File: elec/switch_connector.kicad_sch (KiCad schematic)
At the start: 4 parts, among them J13 BM04B-SRSS-TB, Q2 AO3400A

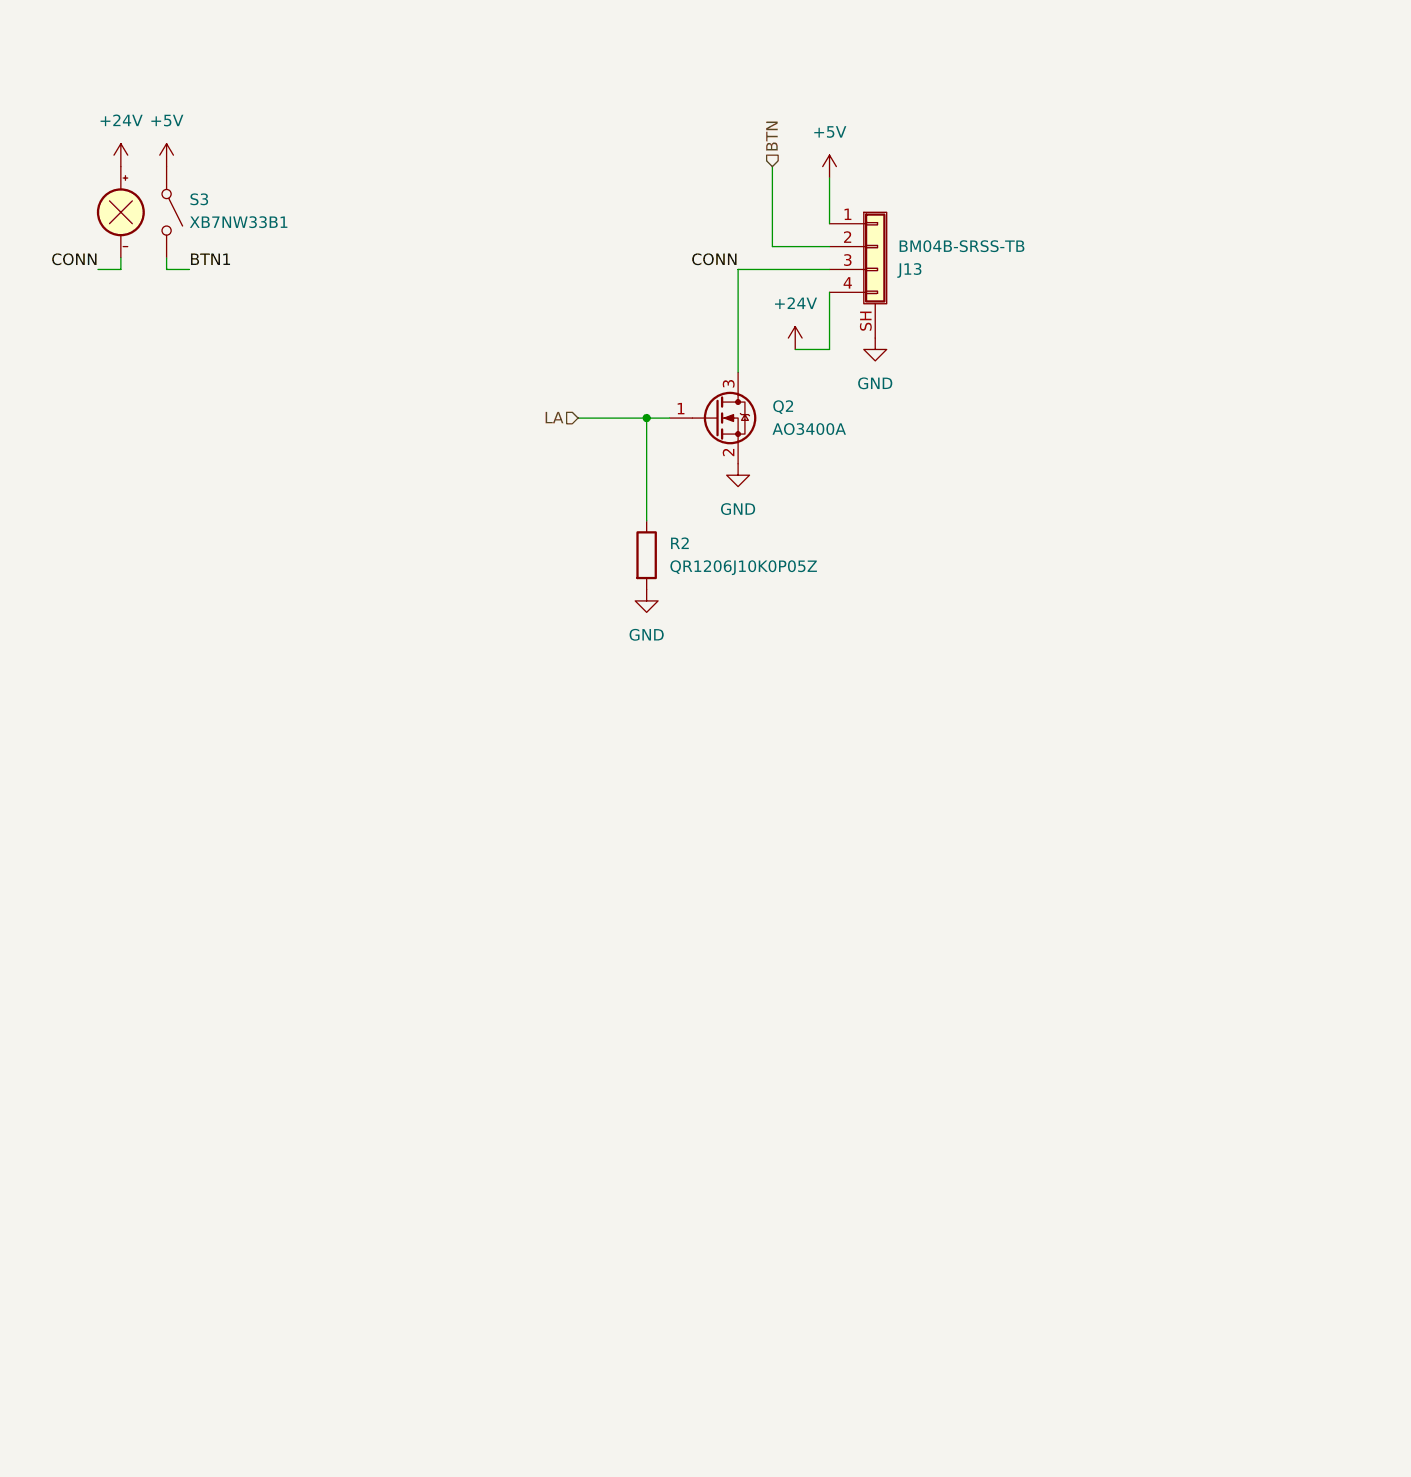
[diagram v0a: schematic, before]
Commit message: feat: adding modularity to PCB
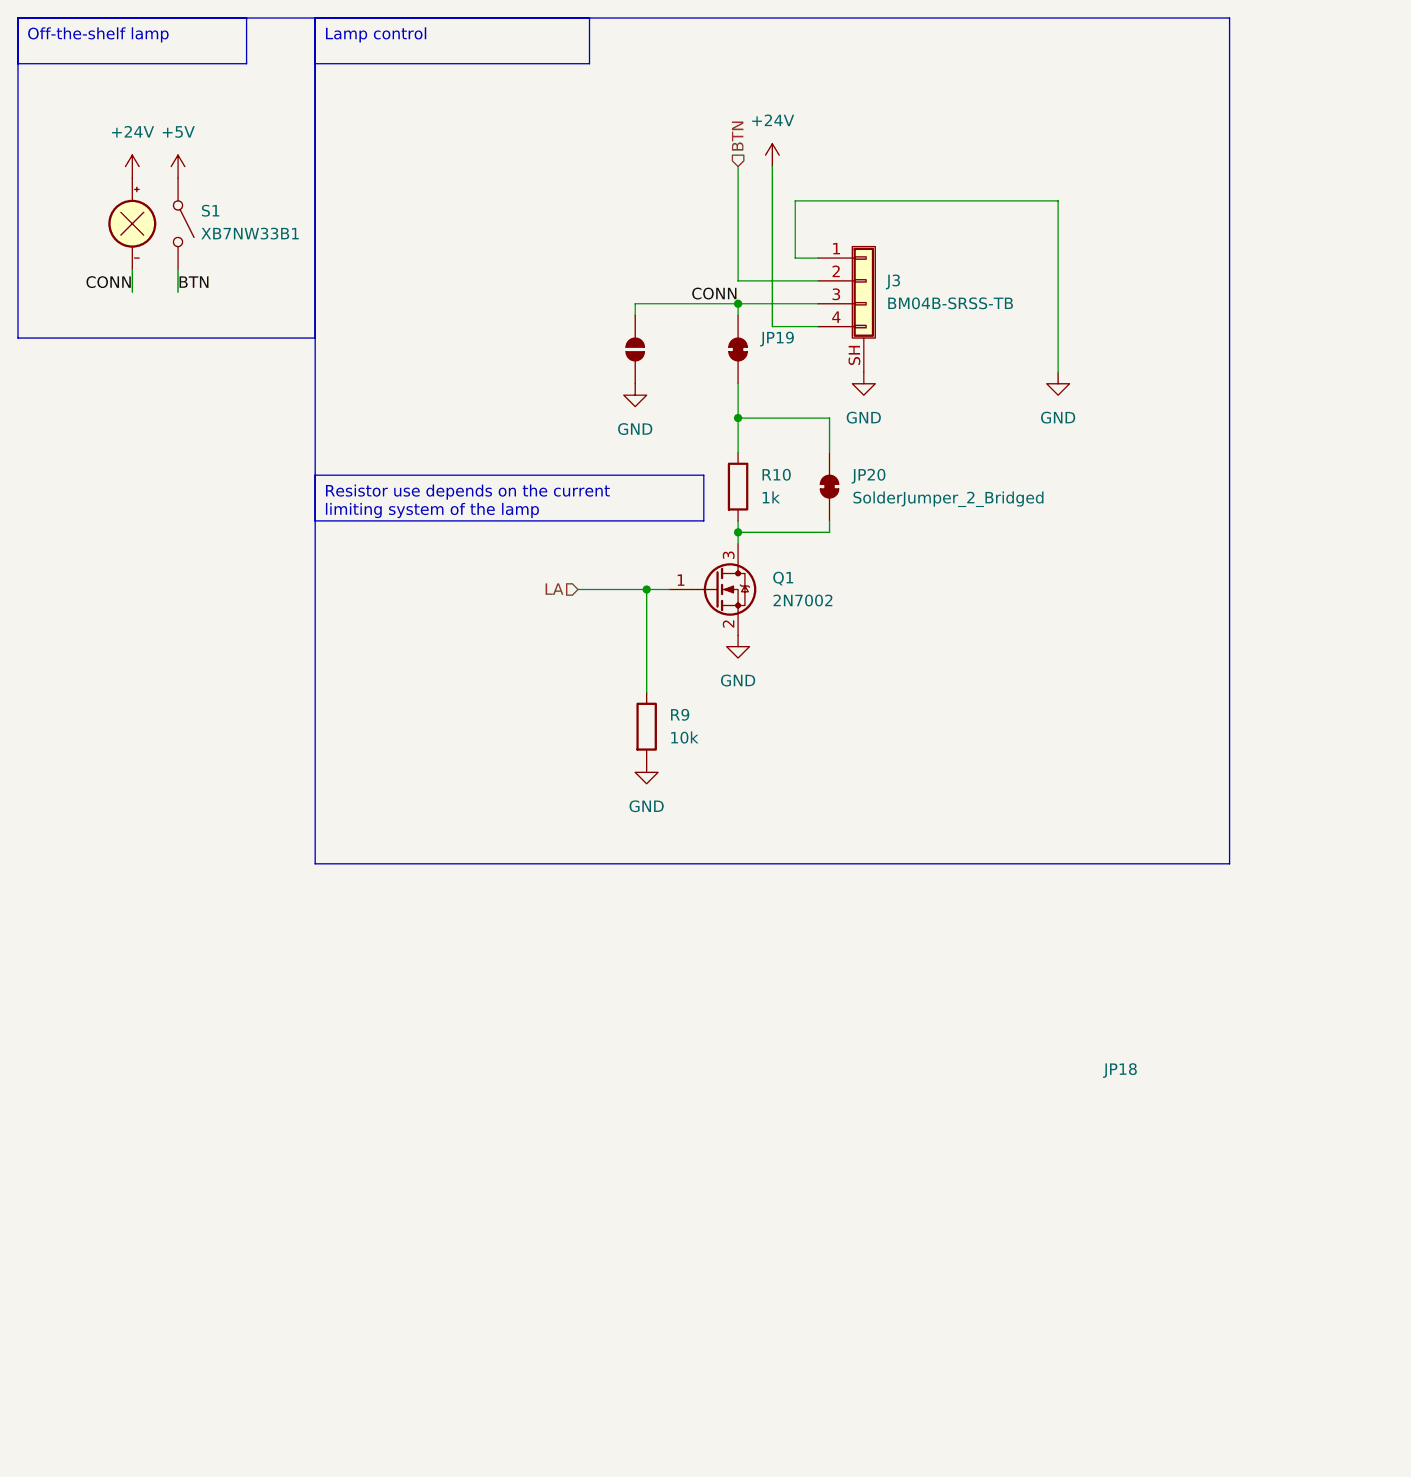
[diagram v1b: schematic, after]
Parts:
- removed Q2: AO3400A, Package_TO_SOT_SMD:SOT-23, symbol Transistor_FET:AO3400A
- added JP18: SolderJumper_2_Open, Jumper:SolderJumper-2_P1.3mm_Open_Pad1.0x1.5mm, symbol Jumper:SolderJumper_2_Open
- added JP19, JP20: SolderJumper_2_Bridged, Jumper:SolderJumper-2_P1.3mm_Bridged_Pad1.0x1.5mm, symbol Jumper:SolderJumper_2_Bridged
- added Q1: 2N7002, Package_TO_SOT_SMD:SOT-23, symbol Transistor_FET:2N7002
- added R10: 1k, Resistor_SMD:R_0805_2012Metric, symbol Device:R
- R9: renamed from R2; value QR1206J10K0P05Z -> 10k; footprint (none) -> Resistor_SMD:R_0805_2012Metric
- renumbered J13 to J3, S3 to S1
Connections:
- net BTN1 is gone; now on net BTN: S1.2 (14)
- net +5V: no longer J3.1 (Pin_1)
- net CONN: now also JP18.1 (A), JP19.2 (B)
- net GND: now also J3.1 (Pin_1), JP18.2 (B), Q1.2 (S)
- net LA: now also Q1.1 (G)
- new net: JP19.1 (A), JP20.2 (B), R10.1
- new net: JP20.1 (A), Q1.3 (D), R10.2
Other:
- moved on the sheet: J3, R9, S1

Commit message: v1 3D print PCB
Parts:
- removed JP19: SolderJumper_2_Bridged, Jumper:SolderJumper-2_P1.3mm_Bridged_Pad1.0x1.5mm, symbol Jumper:SolderJumper_2_Bridged
- renumbered JP20 to JP17
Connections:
- net CONN: now also JP17.2 (B), R10.1; no longer JP18.1 (A)
- net at JP17.1 (A), Q1.3 (D), R10.2: now also JP18.1 (A)
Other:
- moved on the sheet: JP17, JP18, R10

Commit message: doc: outline for fabrication guide
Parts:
- J3: MPN (none) -> C160390
- Q1: MPN (none) -> C8545
- R10: MPN (none) -> C17513
- R9: MPN (none) -> C17414
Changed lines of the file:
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@@
+			)
+		)
+		(property "MPN" "C17414"
+			(at 82.55 91.44 0)
+			(effects
+				(font
+					(size 1.27 1.27)
+				)
+				(hide yes)
 			)
 		)
@@
 			)
 		)
+		(property "MPN" "C8545"
+			(at 90.17 76.2 0)
+			(effects
+				(font
+					(size 1.27 1.27)
+				)
+				(hide yes)
+			)
+		)
 		(pin "1"
 		)
@@
 			)
 		)
+		(property "MPN" "C17513"
+			(at 92.71 63.5 0)
+			(effects
+				(font
+					(size 1.27 1.27)
+				)
+				(hide yes)
+			)
+		)
 		(pin "2"
 		)
@@
 			(at 106.68 41.91 0)
 			(effects
+				(font
+					(size 1.27 1.27)
+				)
+				(hide yes)
+			)
+		)
+		(property "MPN" "C160390"
+			(at 106.68 41.91 0)
+			(effects

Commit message: dev: updating pcb
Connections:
- net +5V is gone; now on net BTN: S1.1 (13)
- net BTN: no longer S1.2 (14)
- net GND: now also S1.2 (14)
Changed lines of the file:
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@@
 	(wire
 		(pts
-			(xy 25.4 43.18) (xy 25.4 40.64)
+			(xy 25.4 45.72) (xy 25.4 40.64)
 		)
 		(stroke
@@
 	(wire
 		(pts
-			(xy 30.48 43.18) (xy 30.48 40.64)
+			(xy 30.48 27.94) (xy 30.48 30.48)
 		)
 		(stroke
@@
 	)
 	(label "BTN"
-		(at 30.48 43.18 0)
+		(at 30.48 27.94 0)
 		(fields_autoplaced yes)
 		(effects
@@
 	)
 	(label "CONN"
-		(at 25.4 43.18 180)
+		(at 25.4 45.72 180)
 		(fields_autoplaced yes)
 		(effects
@@
 	)
 	(symbol
+		(lib_id "power:GND")
+		(at 30.48 40.64 0)
+		(unit 1)
+		(exclude_from_sim no)
+		(in_bom yes)
+		(on_board yes)
+		(dnp no)
+		(fields_autoplaced yes)
+		(property "Reference" "#PWR028"
+			(at 30.48 46.99 0)
+			(effects
+				(font
+					(size 1.27 1.27)
+				)
+				(hide yes)
+			)
+		)
+		(property "Value" "GND"
+			(at 30.48 45.72 0)
+			(effects
+				(font
+					(size 1.27 1.27)
+				)
+			)
+		)
+		(property "Footprint" ""
+			(at 30.48 40.64 0)
+			(effects
+				(font
+					(size 1.27 1.27)
+				)
+				(hide yes)
+			)
+		)
+		(property "Datasheet" ""
+			(at 30.48 40.64 0)
+			(effects
+				(font
+					(size 1.27 1.27)
+				)
+				(hide yes)
+			)
+		)
+		(property "Description" "Power symbol creates a global label with name \"GND\" , ground"
+			(at 30.48 40.64 0)
+			(effects
+				(font
+					(size 1.27 1.27)
+				)
+				(hide yes)
+			)
+		)
+		(pin "1"
+		)
+		(instances
+			(project "elec"
+				(path "/9721bce9-01f4-4230-bc1e-748d0303b61d/d1c63f12-a9c6-44fc-aada-0b6e04e33293"
+					(reference "#PWR028")
+					(unit 1)
+				)
+				(path "/9721bce9-01f4-4230-bc1e-748d0303b61d/5ed1a42c-1f8a-456f-aca4-b0ec53e5043f"
+					(reference "#PWR036")
+					(unit 1)
+				)
+				(path "/9721bce9-01f4-4230-bc1e-748d0303b61d/fdf19939-3d9b-4110-9022-c37157a29402"
+					(reference "#PWR044")
+					(unit 1)
+				)
+				(path "/9721bce9-01f4-4230-bc1e-748d0303b61d/37f927af-89ef-4fdd-8956-bca34548d96f"
+					(reference "#PWR052")
+					(unit 1)
+				)
+				(path "/9721bce9-01f4-4230-bc1e-748d0303b61d/986b1860-5bd6-47a5-b66e-b737b7bd0f11"
+					(reference "#PWR060")
+					(unit 1)
+				)
+				(path "/9721bce9-01f4-4230-bc1e-748d0303b61d/eebd9391-916f-49b6-bec7-88d6969a1573"
+					(reference "#PWR068")
+					(unit 1)
+				)
+				(path "/9721bce9-01f4-4230-bc1e-748d0303b61d/d67cbc77-a7b3-4445-bb70-2db77a7feb74"
+					(reference "#PWR076")
+					(unit 1)
+				)
+				(path "/9721bce9-01f4-4230-bc1e-748d0303b61d/3bc99195-9e3c-4290-911f-d629015a354c"
+					(reference "#PWR084")
+					(unit 1)
+				)
+				(path "/9721bce9-01f4-4230-bc1e-748d0303b61d/e3e2ca04-3651-46d9-8ec0-5b3aca5c73d2"
+					(reference "#PWR092")
+					(unit 1)
+				)
+				(path "/9721bce9-01f4-4230-bc1e-748d0303b61d/333f48b8-09d6-4cfc-b48e-393e968338e9"
+					(reference "#PWR0100")
+					(unit 1)
+				)
+			)
+		)
+	)
+	(symbol
 		(lib_id "breakout:XB7NW33B1")
 		(at 30.48 35.56 0)
@@
 					(unit 1)
 				)
-			)
-		)
-	)
-	(symbol
-		(lib_id "power:+5V")
-		(at 30.48 30.48 0)
-		(unit 1)
-		(exclude_from_sim no)
-		(in_bom yes)
-		(on_board yes)
-		(dnp no)
-		(fields_autoplaced yes)
-		(property "Reference" "#PWR028"
-			(at 30.48 34.29 0)
-			(effects
-				(font
-					(size 1.27 1.27)
-				)
-				(hide yes)
-			)
-		)
-		(property "Value" "+5V"
-			(at 30.48 25.4 0)
-			(effects
-				(font
-					(size 1.27 1.27)
-				)
-			)
-		)
-		(property "Footprint" ""
-			(at 30.48 30.48 0)
-			(effects
-				(font
-					(size 1.27 1.27)
-				)
-				(hide yes)
-			)
-		)
-		(property "Datasheet" ""
-			(at 30.48 30.48 0)
-			(effects
-				(font
-					(size 1.27 1.27)
-				)
-				(hide yes)
-			)
-		)
-		(property "Description" "Power symbol creates a global label with name \"+5V\""
-			(at 30.48 30.48 0)
-			(effects
-				(font
-					(size 1.27 1.27)
-				)
-				(hide yes)
-			)
-		)
-		(pin "1"
-		)
-		(instances
-			(project "elec"
-				(path "/9721bce9-01f4-4230-bc1e-748d0303b61d/d1c63f12-a9c6-44fc-aada-0b6e04e33293"
-					(reference "#PWR028")
-					(unit 1)
-				)
-				(path "/9721bce9-01f4-4230-bc1e-748d0303b61d/5ed1a42c-1f8a-456f-aca4-b0ec53e5043f"
-					(reference "#PWR036")
-					(unit 1)
-				)
-				(path "/9721bce9-01f4-4230-bc1e-748d0303b61d/fdf19939-3d9b-4110-9022-c37157a29402"
-					(reference "#PWR044")
-					(unit 1)
-				)
-				(path "/9721bce9-01f4-4230-bc1e-748d0303b61d/37f927af-89ef-4fdd-8956-bca34548d96f"
-					(reference "#PWR052")
-					(unit 1)
-				)
-				(path "/9721bce9-01f4-4230-bc1e-748d0303b61d/986b1860-5bd6-47a5-b66e-b737b7bd0f11"
-					(reference "#PWR060")
-					(unit 1)
-				)
-				(path "/9721bce9-01f4-4230-bc1e-748d0303b61d/eebd9391-916f-49b6-bec7-88d6969a1573"
-					(reference "#PWR068")
-					(unit 1)
-				)
-				(path "/9721bce9-01f4-4230-bc1e-748d0303b61d/d67cbc77-a7b3-4445-bb70-2db77a7feb74"
-					(reference "#PWR076")
-					(unit 1)
-				)
-				(path "/9721bce9-01f4-4230-bc1e-748d0303b61d/3bc99195-9e3c-4290-911f-d629015a354c"
-					(reference "#PWR084")
-					(unit 1)
-				)
-				(path "/9721bce9-01f4-4230-bc1e-748d0303b61d/e3e2ca04-3651-46d9-8ec0-5b3aca5c73d2"
-					(reference "#PWR092")
-					(unit 1)
-				)
-				(path "/9721bce9-01f4-4230-bc1e-748d0303b61d/333f48b8-09d6-4cfc-b48e-393e968338e9"
-					(reference "#PWR0100")
-					(unit 1)
-				)
